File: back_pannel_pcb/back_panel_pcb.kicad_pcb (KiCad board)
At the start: 2 copper layers, 93.3 x 100 mm, 8 parts

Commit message: add artwork
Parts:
- added G***: LOGO, PL_logo:logo_height_20mm, F.Cu at (100.0, 100.0)
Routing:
- net (no net): track 0.00 -> 7359.2 mm
- added copper zone on B.Cu, net (none)
- added copper zone on F.Cu, net (none)
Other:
- board text added: "Base Convert Back Panel PCB github.com/sdp8483/base_convert Sam Perry July 2018"

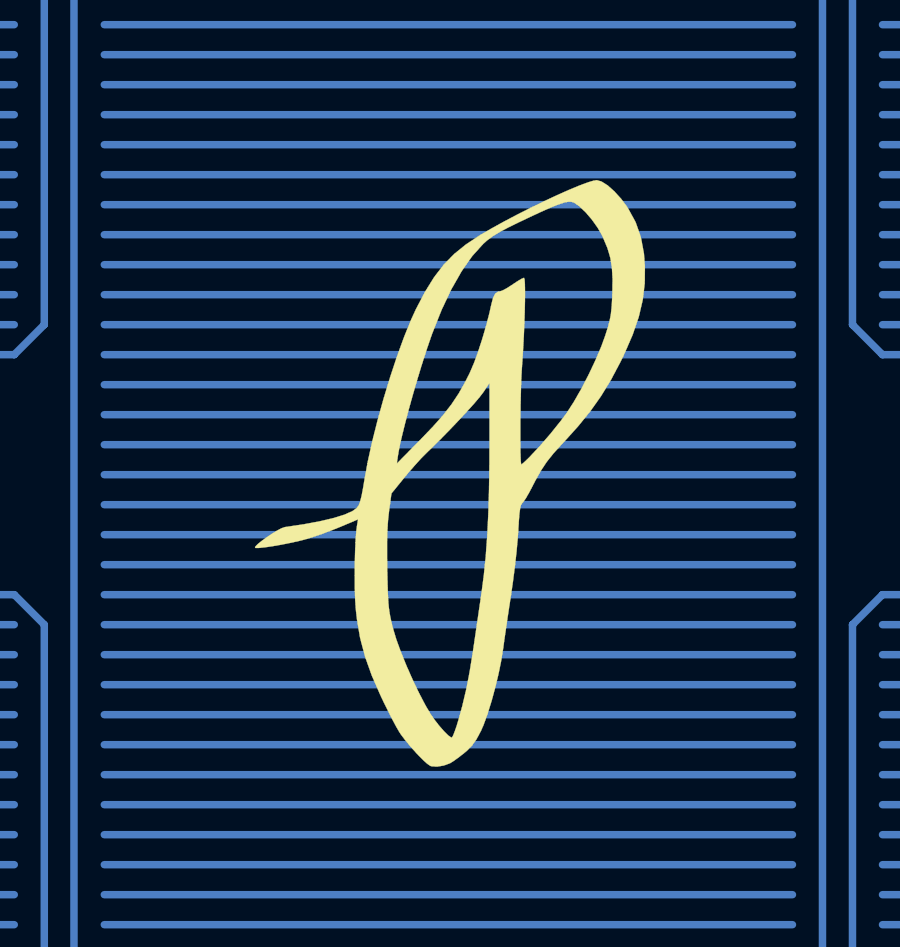
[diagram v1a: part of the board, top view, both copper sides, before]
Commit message: added silkscreen to back
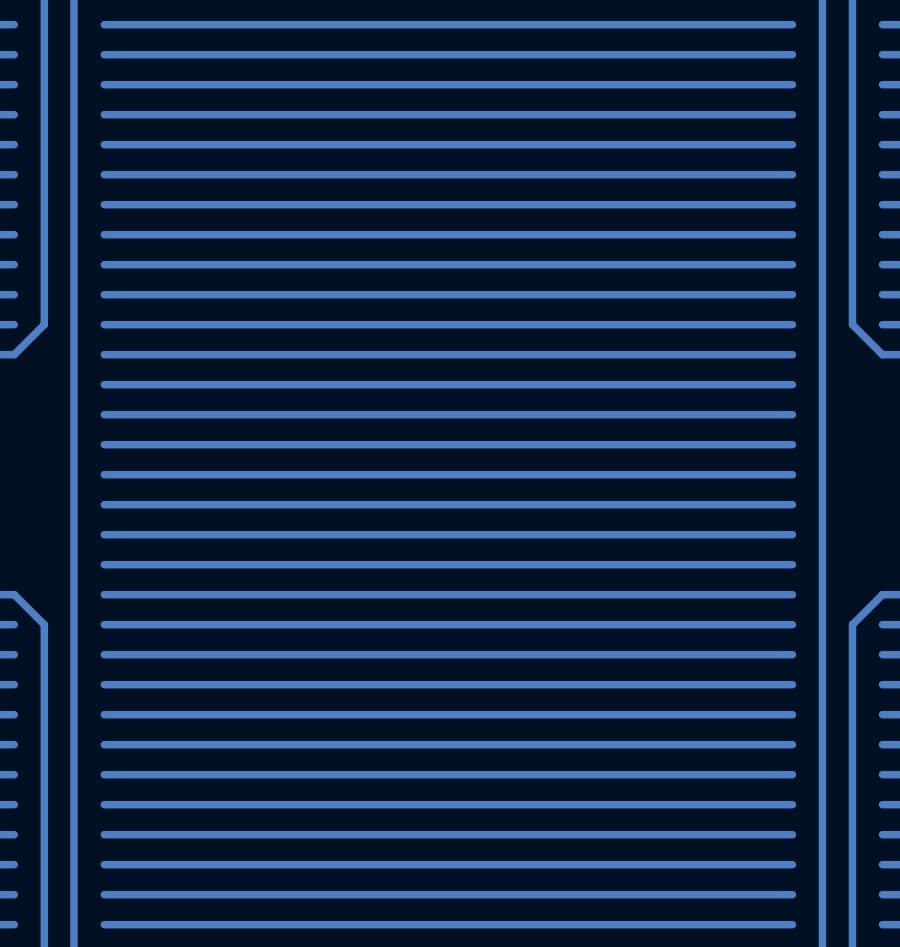
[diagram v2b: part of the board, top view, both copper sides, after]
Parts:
- removed G***: LOGO, PL_logo:logo_height_20mm
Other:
- board text added: "Base Convert"
- board text added: "Sam Perry July 2018"
